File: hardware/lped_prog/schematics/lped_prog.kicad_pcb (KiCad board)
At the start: 2 copper layers, 48 x 15 mm, 12 parts, among them J1 J-Link Header, J2 Conn_01x01_Pin, J3 Conn_01x01_Pin, J4 Conn_01x01_Pin, J5 Conn_01x01_Pin, J6 Conn_01x01_Pin, J7 Conn_01x01_Pin

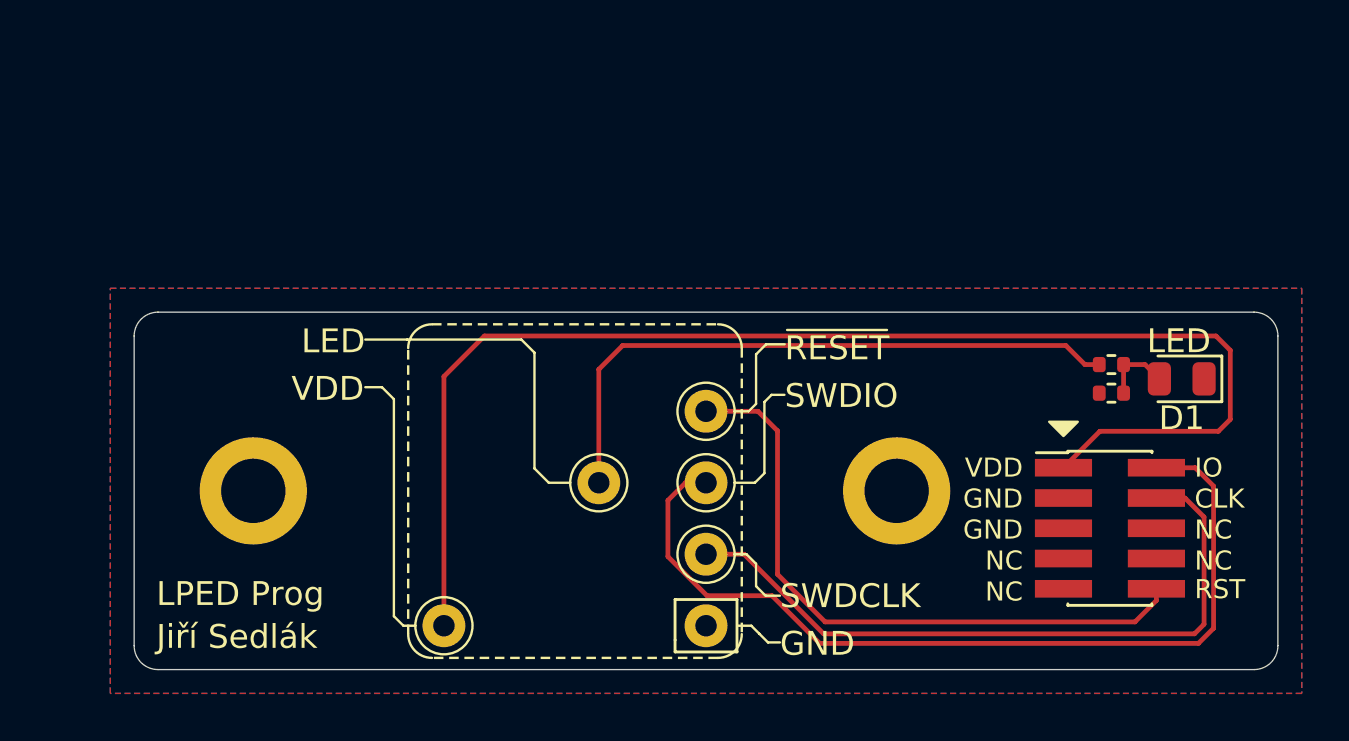
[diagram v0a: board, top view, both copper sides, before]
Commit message: feat(hardware): added usb and manual input to programmer, added reset button and connection switch
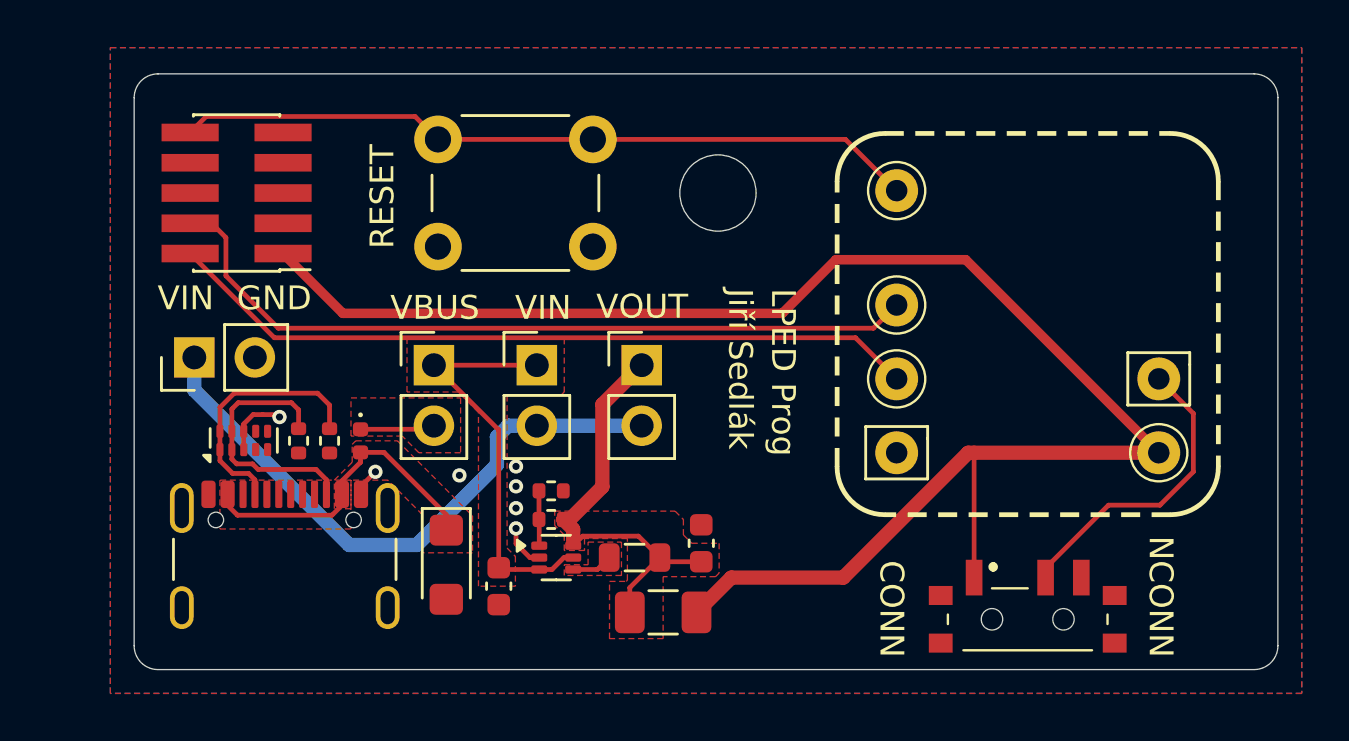
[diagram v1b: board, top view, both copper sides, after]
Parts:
- removed H2: M3, MountingHole:MountingHole_2.7mm_M2.5_ISO7380_Pad
- added C2: 10u, Capacitor_SMD:C_0603_1608Metric, F.Cu at (117.3, 86.5)
- added C3: 10u, Capacitor_SMD:C_0603_1608Metric, F.Cu at (125.8, 84.7)
- added D2: D_Small, Diode_SMD:D_0402_1005Metric, F.Cu at (111.5, 80.4)
- added F1: Polyfuse_Small, Fuse:Fuse_1206_3216Metric, F.Cu at (124.2, 87.6)
- added J8: Power connector, Connector_PinHeader_2.54mm:PinHeader_1x02_P2.54mm_Vertical, F.Cu at (104.5, 76.9)
- added J9: Conn_01x01_Pin, Connector_Pin:Pin_D0.9mm_L10.0mm_W2.4mm_FlatFork, F.Cu at (145.0, 77.8)
- added JP2: VIN_REG, Connector_PinHeader_2.54mm:PinHeader_1x02_P2.54mm_Vertical, F.Cu at (118.9, 77.2)
- added JP3: VBUS_REG, Connector_PinHeader_2.54mm:PinHeader_1x02_P2.54mm_Vertical, F.Cu at (114.6, 77.2)
- added JP4: VIN_NREG, Connector_PinHeader_2.54mm:PinHeader_1x02_P2.54mm_Vertical, F.Cu at (123.3, 77.2)
- added L1: 1uH, Inductor_SMD:L_0805_2012Metric, F.Cu at (123.0, 85.3)
- added R3: 5k1, Resistor_SMD:R_0402_1005Metric, F.Cu at (110.2, 80.4)
- added R4: 5k1, Resistor_SMD:R_0402_1005Metric, F.Cu at (108.9, 80.4)
- added SW1: Connection toggle, Switches_Toggles:EG1215AA, F.Cu at (139.5, 87.9)
- added SW2: Reset switch, Button_Switch_THT:SW_PUSH_6mm_H4.3mm, F.Cu at (114.8, 67.8)
- added U2: TPD4E02B04DQA, Package_SON:USON-10_2.5x1.0mm_P0.5mm, F.Cu at (106.6, 80.4)
- added U3: AP61100, Package_TO_SOT_SMD:SOT-563, F.Cu at (119.7, 85.3)
- D1: value LED -> SMF22A; footprint Diode_SMD:D_0805_2012Metric -> Diode_SMD:D_SMF
- H1: value M3 -> MountingHole; footprint MountingHole:MountingHole_2.7mm_M2.5_ISO7380_Pad -> MountingHole:MountingHole_3.2mm_M3
- J7: value Conn_01x01_Pin -> USB_C_Receptacle_USB2.0_14P; footprint Connector_Pin:Pin_D0.9mm_L10.0mm_W2.4mm_FlatFork -> Connector_USB:USB_C_Receptacle_GCT_USB4105-xx-A_16P_TopMnt_Horizontal
- R1: value 2k1 -> 200k
- R2: value 10k -> 44k2
- moved J1 39.3 mm to (106.3, 70.0), turned to 180 degrees
- moved D1 31.8 mm to (115.1, 85.6), turned to -90 degrees
- moved J3 30.9 mm to (145.0, 80.9), turned to 180 degrees
- moved R1 24.4 mm to (119.5, 83.7), turned to 180 degrees
- moved R2 23.9 mm to (119.5, 82.5)
- moved H1 14.6 mm to (126.5, 70.0)
- moved J7 13.8 mm to (108.3, 86.3)
- moved J5 13.2 mm to (134.0, 74.7), turned to 180 degrees
- moved J6 12.2 mm to (134.0, 69.9), turned to 180 degrees
- moved J2 10.8 mm to (134.0, 80.9), turned to 180 degrees
- moved J4 9.11 mm to (134.0, 77.8), turned to 180 degrees
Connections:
- D1 pad 1: Earth -> VBUS
- D1 pad 2: Net-(D1-A) -> Earth
- R1 pad 1: /LED -> Net-(JP4-A)
- R1 pad 2: Net-(D1-A) -> Net-(U3-FB)
- R2 pad 1: Earth -> Net-(U3-FB)
- R2 pad 2: Net-(D1-A) -> Earth
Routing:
- net /LED: track 26.5 -> 0.00 mm
- net VIN: track 0.00 -> 25.6 mm
- net Net-(JP4-A): track 0.00 -> 18.4 mm
- net Net-(JP2-A): track 0.00 -> 17.4 mm
- net /VDD: track 55.2 -> 69.5 mm
- net VBUS: track 0.00 -> 13.5 mm
- net /CONN: track 0.00 -> 12.8 mm
- net /CC2: track 0.00 -> 10.9 mm
- net /CC1: track 0.00 -> 10.7 mm
- net Earth: track 0.00 -> 5.89 mm, vias 0 -> 7
- net /SWDIO: track 37.6 -> 31.8 mm
- net /~{RESET}: track 27.0 -> 31.2 mm
- net /SWDCLK: track 29.3 -> 32.8 mm
- net Net-(D2-K): track 0.00 -> 3.14 mm
- net Net-(D1-A): track 2.95 -> 0.00 mm
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- added copper zone on F.Cu, net Net-(D2-K)
- added copper zone on F.Cu, net Net-(JP2-A)
- added copper zone on F.Cu, net Net-(JP4-A)
- added copper zone on F.Cu, net Net-(U3-SW)
- added copper zone on F.Cu, net VBUS
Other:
- board size 48 x 15 mm -> 48 x 25 mm
- board text added: "CONN"
- board text added: "NCONN"
- board text added: "RESET"
- board text added: "VBUS"
- board text added: "VIN"
- board text added: "VOUT"
- board text removed: "CLK"
- board text removed: "IO"
- board text removed: "LED"
- board text removed: "NC"
- board text removed: "RST"
- board text removed: "SWDCLK"
- board text removed: "SWDIO"
- board text removed: "VDD"
- board text removed: "~{RESET}"

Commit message: feat(hardware): added stiching to programmer
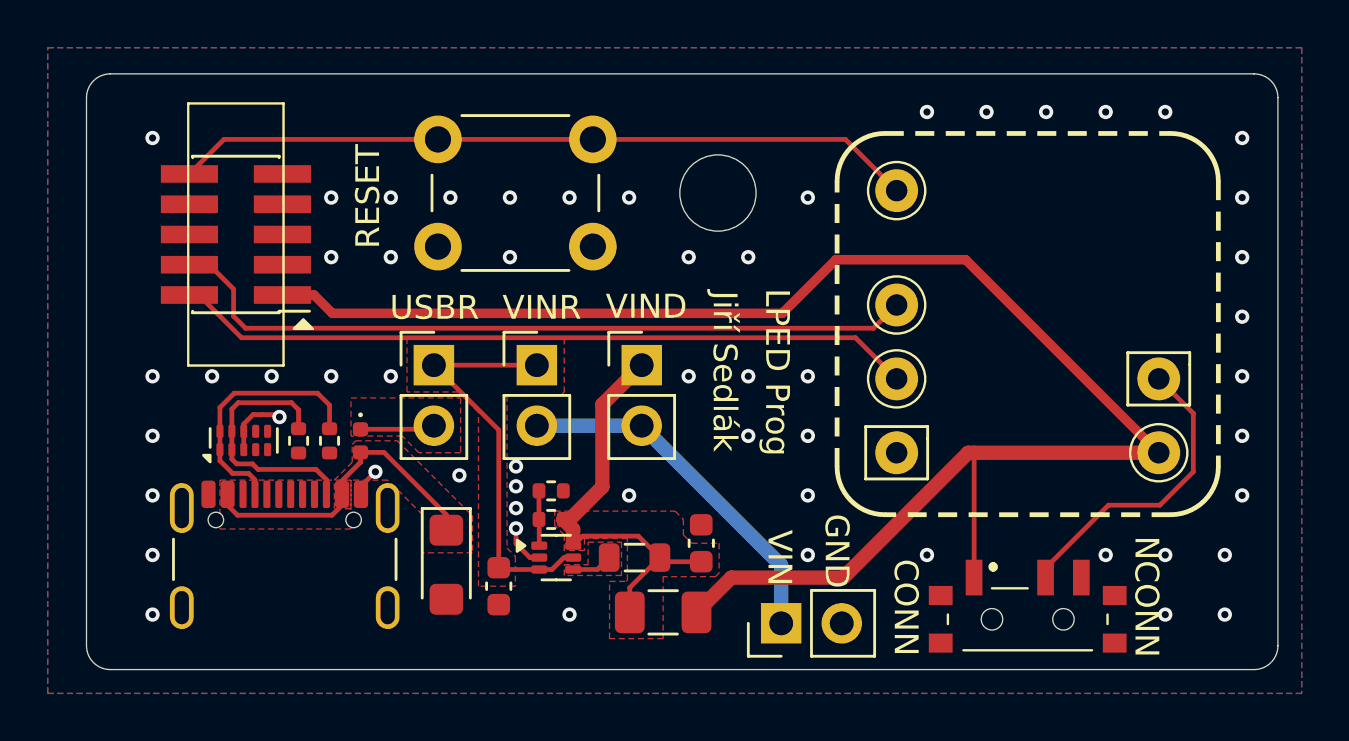
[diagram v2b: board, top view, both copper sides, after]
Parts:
- moved J8 27.0 mm to (129.2, 88.1)
- moved J1 1.74 mm to (106.3, 71.7)
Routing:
- net VIN: track 25.6 -> 15.1 mm
- net /SWDCLK: track 32.8 -> 31.9 mm
- net /VDD: track 69.5 -> 68.8 mm
- net /SWDIO: track 31.8 -> 31.1 mm
- net Earth: vias 7 -> 56
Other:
- board size 48 x 25 mm -> 50 x 25 mm
- board text added: "USBR"
- board text added: "VIND"
- board text added: "VINR"
- board text removed: "VBUS"
- board text removed: "VOUT"

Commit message: feat(hardware): chaged regulator
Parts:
- removed U3: AP61100, Package_TO_SOT_SMD:SOT-563
- added U1: TLV62080DSGx, Package_SON:WSON-8-1EP_2x2mm_P0.5mm_EP0.9x1.6mm, F.Cu at (119.5, 85.0)
- L1: footprint Inductor_SMD:L_0805_2012Metric -> Inductor_SMD:L_1008_2520Metric
- R1: value 200k -> 43k
- R2: value 44k2 -> 33k
- moved C3 6.92 mm to (119.4, 87.4), turned to 180 degrees
- moved R1 4.58 mm to (117.1, 87.6), turned to 90 degrees
- moved C2 4.28 mm to (119.5, 82.8), turned to 0 degrees
- moved R2 3.65 mm to (117.1, 85.2), turned to 90 degrees
- moved F1 2.78 mm to (125.9, 85.4), turned to -90 degrees
- moved D1 0.55 mm to (115.1, 86.2)
- moved L1 0.40 mm to (123.0, 85.7), turned to -90 degrees
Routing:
- net Net-(JP4-A): track 18.4 -> 21.6 mm
- net Net-(JP2-A): track 17.4 -> 14.7 mm
- net Earth: track 5.89 -> 3.98 mm
- net Net-(U1-SW): track 1.72 -> 2.57 mm
- net /VDD: track 68.8 -> 68.2 mm
- net Net-(U1-FB): track 2.32 -> 2.85 mm
